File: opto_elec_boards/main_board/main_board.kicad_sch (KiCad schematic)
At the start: 21 parts, among them J1 IN1_BNC, J10 Conn_02x10_Odd_Even, J2 IN2_BNC, J3 OUT1_BNC, J4 OUT2_BNC, J5 OUT3_BNC, J6 OUT4_BNC, J7 Conn_01x02, J8 Conn_01x02, U1 L7805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

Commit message: Update OptoElec Board / Main board
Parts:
- added J11: SWITCH_B, Connector_PinSocket_2.54mm:PinSocket_1x03_P2.54mm_Vertical, symbol Connector_Generic:Conn_01x03
- added J12: SWITCH_C, Connector_PinSocket_2.54mm:PinSocket_1x03_P2.54mm_Vertical, symbol Connector_Generic:Conn_01x03
- added J9: SWITCH_A, Connector_PinSocket_2.54mm:PinSocket_1x03_P2.54mm_Vertical, symbol Connector_Generic:Conn_01x03
- added R1, R2, R3: 8.2k, Resistor_THT:R_Axial_DIN0207_L6.3mm_D2.5mm_P10.16mm_Horizontal, symbol Device:R
- J10: value Conn_02x10_Odd_Even -> To Slave Board
- J7: value Conn_01x02 -> POW_+15V; footprint TerminalBlock_Phoenix:TerminalBlock_Phoenix_MKDS-3-2-5.08_1x02_P5.08mm_Horizontal -> Connector_PinSocket_2.54mm:PinSocket_1x02_P2.54mm_Vertical
- J8: value Conn_01x02 -> POW_-15V; footprint TerminalBlock_Phoenix:TerminalBlock_Phoenix_MKDS-3-2-5.08_1x02_P5.08mm_Horizontal -> Connector_PinSocket_2.54mm:PinSocket_1x02_P2.54mm_Vertical
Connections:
- net +15V: now also J10.2 (Pin_2); no longer J10.7 (Pin_7)
- net -15V: now also J10.4 (Pin_4); no longer J10.9 (Pin_9)
- net 3.3V: now also J11.3 (Pin_3), J12.3 (Pin_3), J9.3 (Pin_3)
- net GND: now also J10.12 (Pin_12), J10.20 (Pin_20), J10.6 (Pin_6), J11.1 (Pin_1), J12.1 (Pin_1), J9.1 (Pin_1), R1.2, R2.2, R3.2; no longer J10.10 (Pin_10), J10.11 (Pin_11), J10.14 (Pin_14)
- net OUT1: now also J10.13 (Pin_13); no longer J10.2 (Pin_2)
- net OUT2: now also J10.11 (Pin_11); no longer J10.4 (Pin_4)
- net OUT3: now also J10.9 (Pin_9); no longer J10.6 (Pin_6)
- net OUT4: now also J10.7 (Pin_7); no longer J10.8 (Pin_8)
- net RVAR_3.3V: now also J10.8 (Pin_8); no longer J10.13 (Pin_13)
- net RVAR_5V: now also J10.10 (Pin_10); no longer J10.12 (Pin_12)
- net SEL1: now also J10.18 (Pin_18), J9.2 (Pin_2), R1.1; no longer J10.20 (Pin_20)
- net SEL2: now also J10.16 (Pin_16), J11.2 (Pin_2), R2.1; no longer J10.18 (Pin_18)
- net SEL3: now also J10.14 (Pin_14), J12.2 (Pin_2), R3.1; no longer J10.16 (Pin_16)

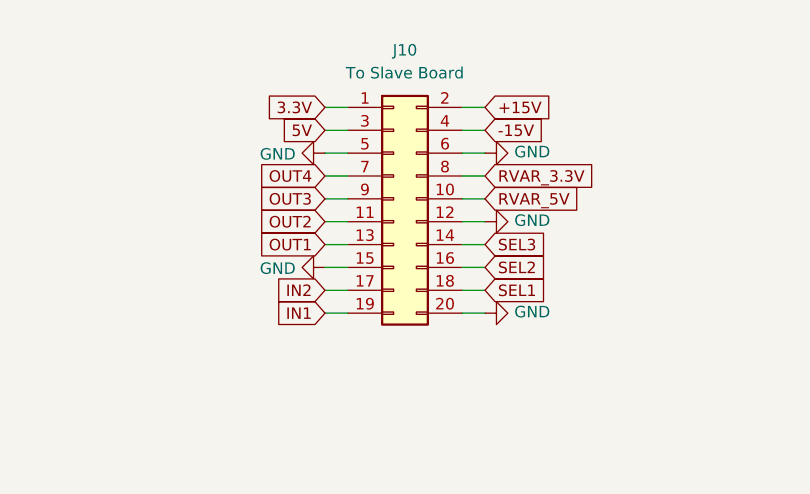
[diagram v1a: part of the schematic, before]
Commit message: Update Opto new boards / Main and PhotoSlave
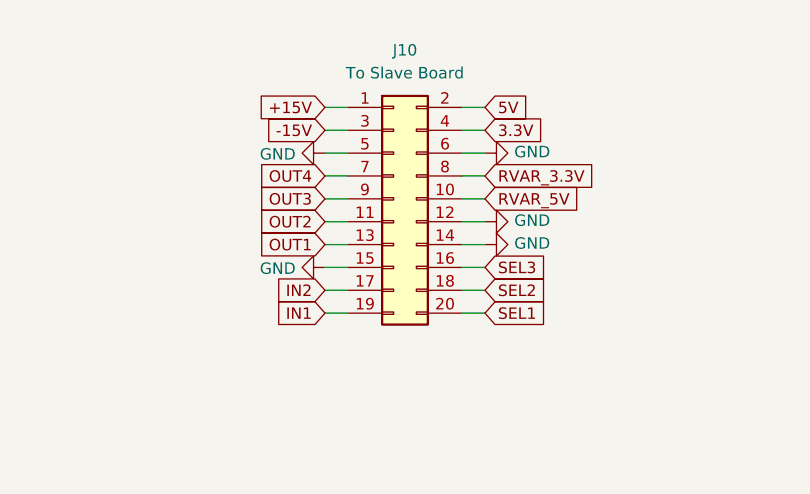
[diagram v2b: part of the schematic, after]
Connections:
- net +15V: now also J10.1 (Pin_1); no longer J10.2 (Pin_2)
- net -15V: now also J10.3 (Pin_3); no longer J10.4 (Pin_4)
- net 3.3V: now also J10.4 (Pin_4); no longer J10.1 (Pin_1)
- net 5V: now also J10.2 (Pin_2); no longer J10.3 (Pin_3)
- net GND: now also J10.14 (Pin_14); no longer J10.20 (Pin_20)
- net SEL1: now also J10.20 (Pin_20); no longer J10.18 (Pin_18)
- net SEL2: now also J10.18 (Pin_18); no longer J10.16 (Pin_16)
- net SEL3: now also J10.16 (Pin_16); no longer J10.14 (Pin_14)
